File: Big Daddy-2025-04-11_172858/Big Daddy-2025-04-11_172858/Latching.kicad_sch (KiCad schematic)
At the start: 12 parts, among them J1 BMS Button, J2 IMD Button, K2 G5V-2, K3 G5V-2

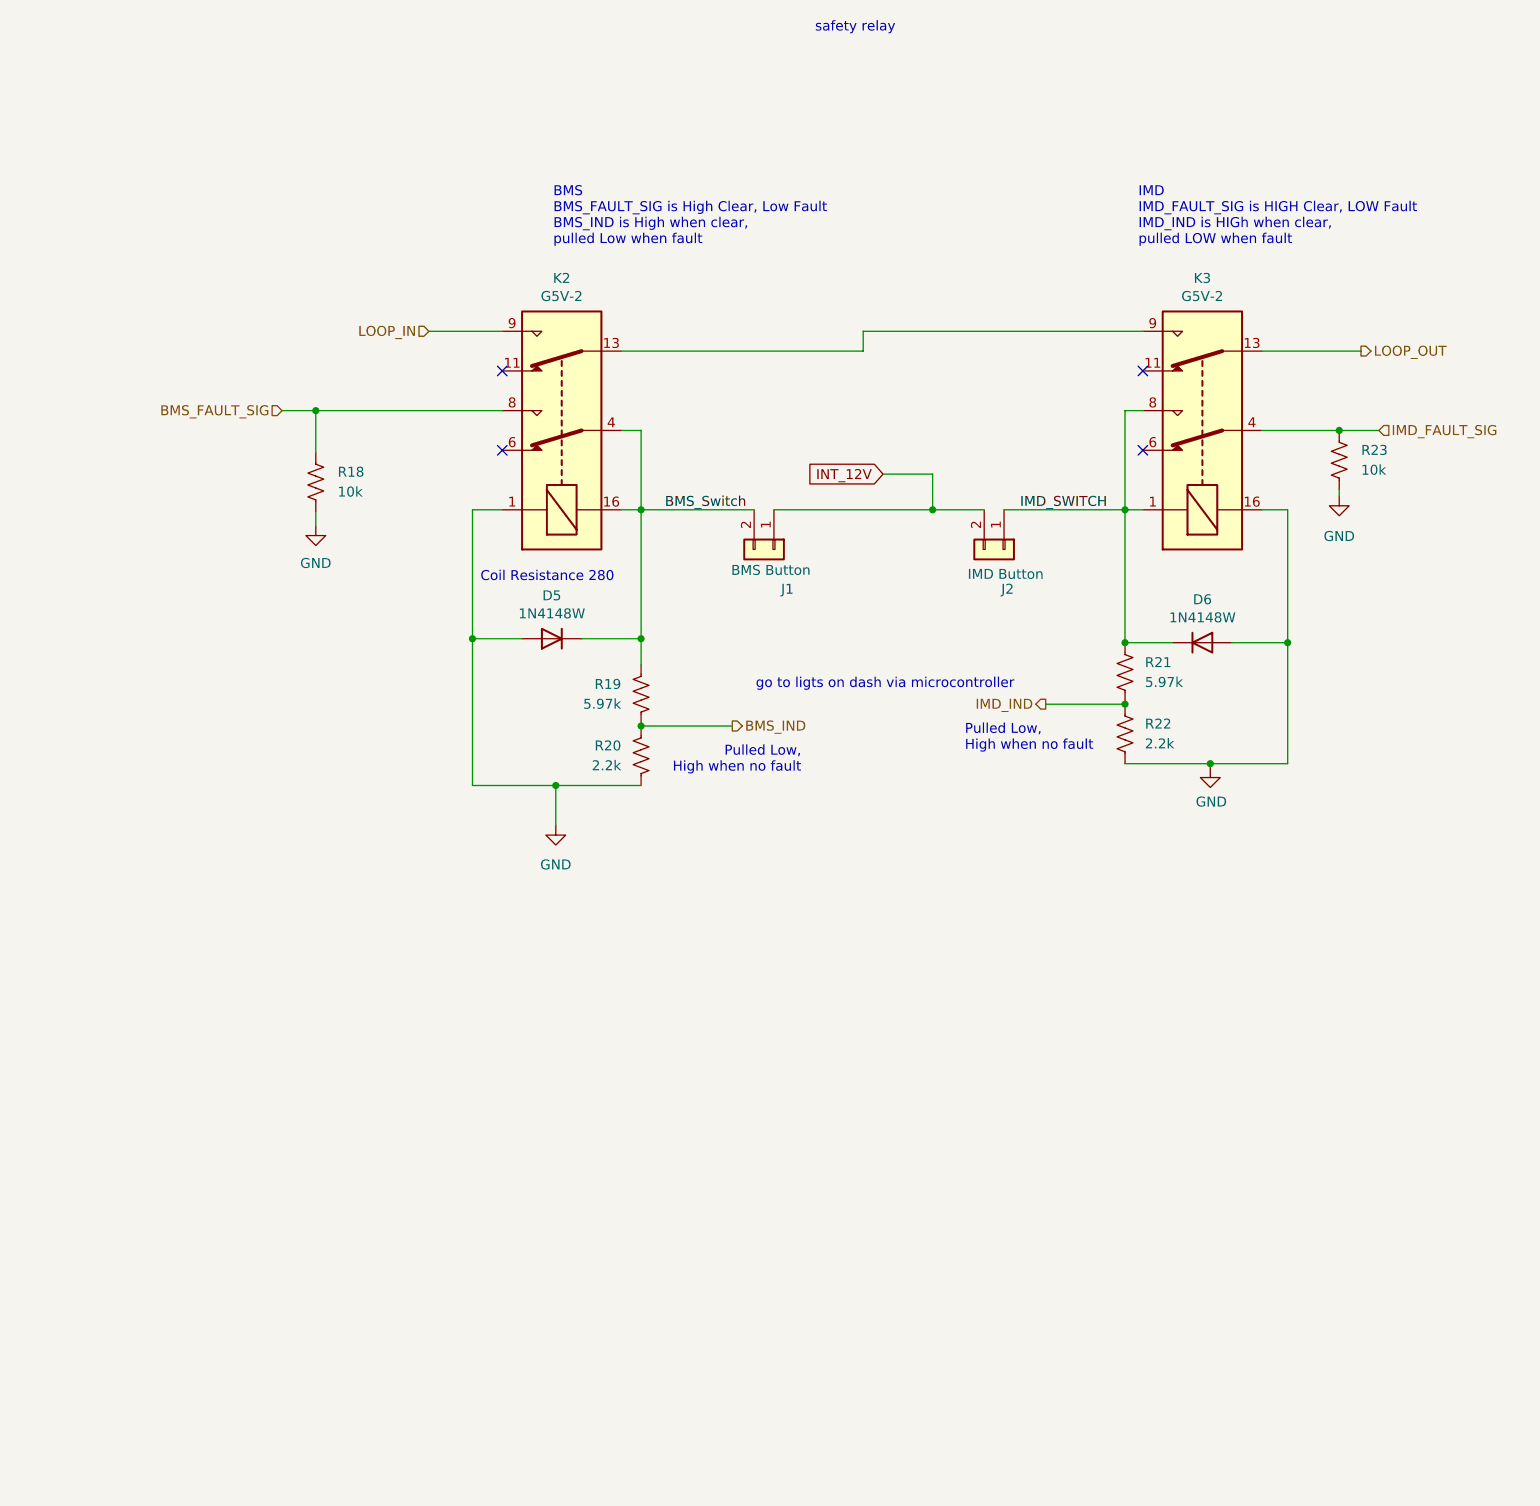
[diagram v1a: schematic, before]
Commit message: changed bms relay
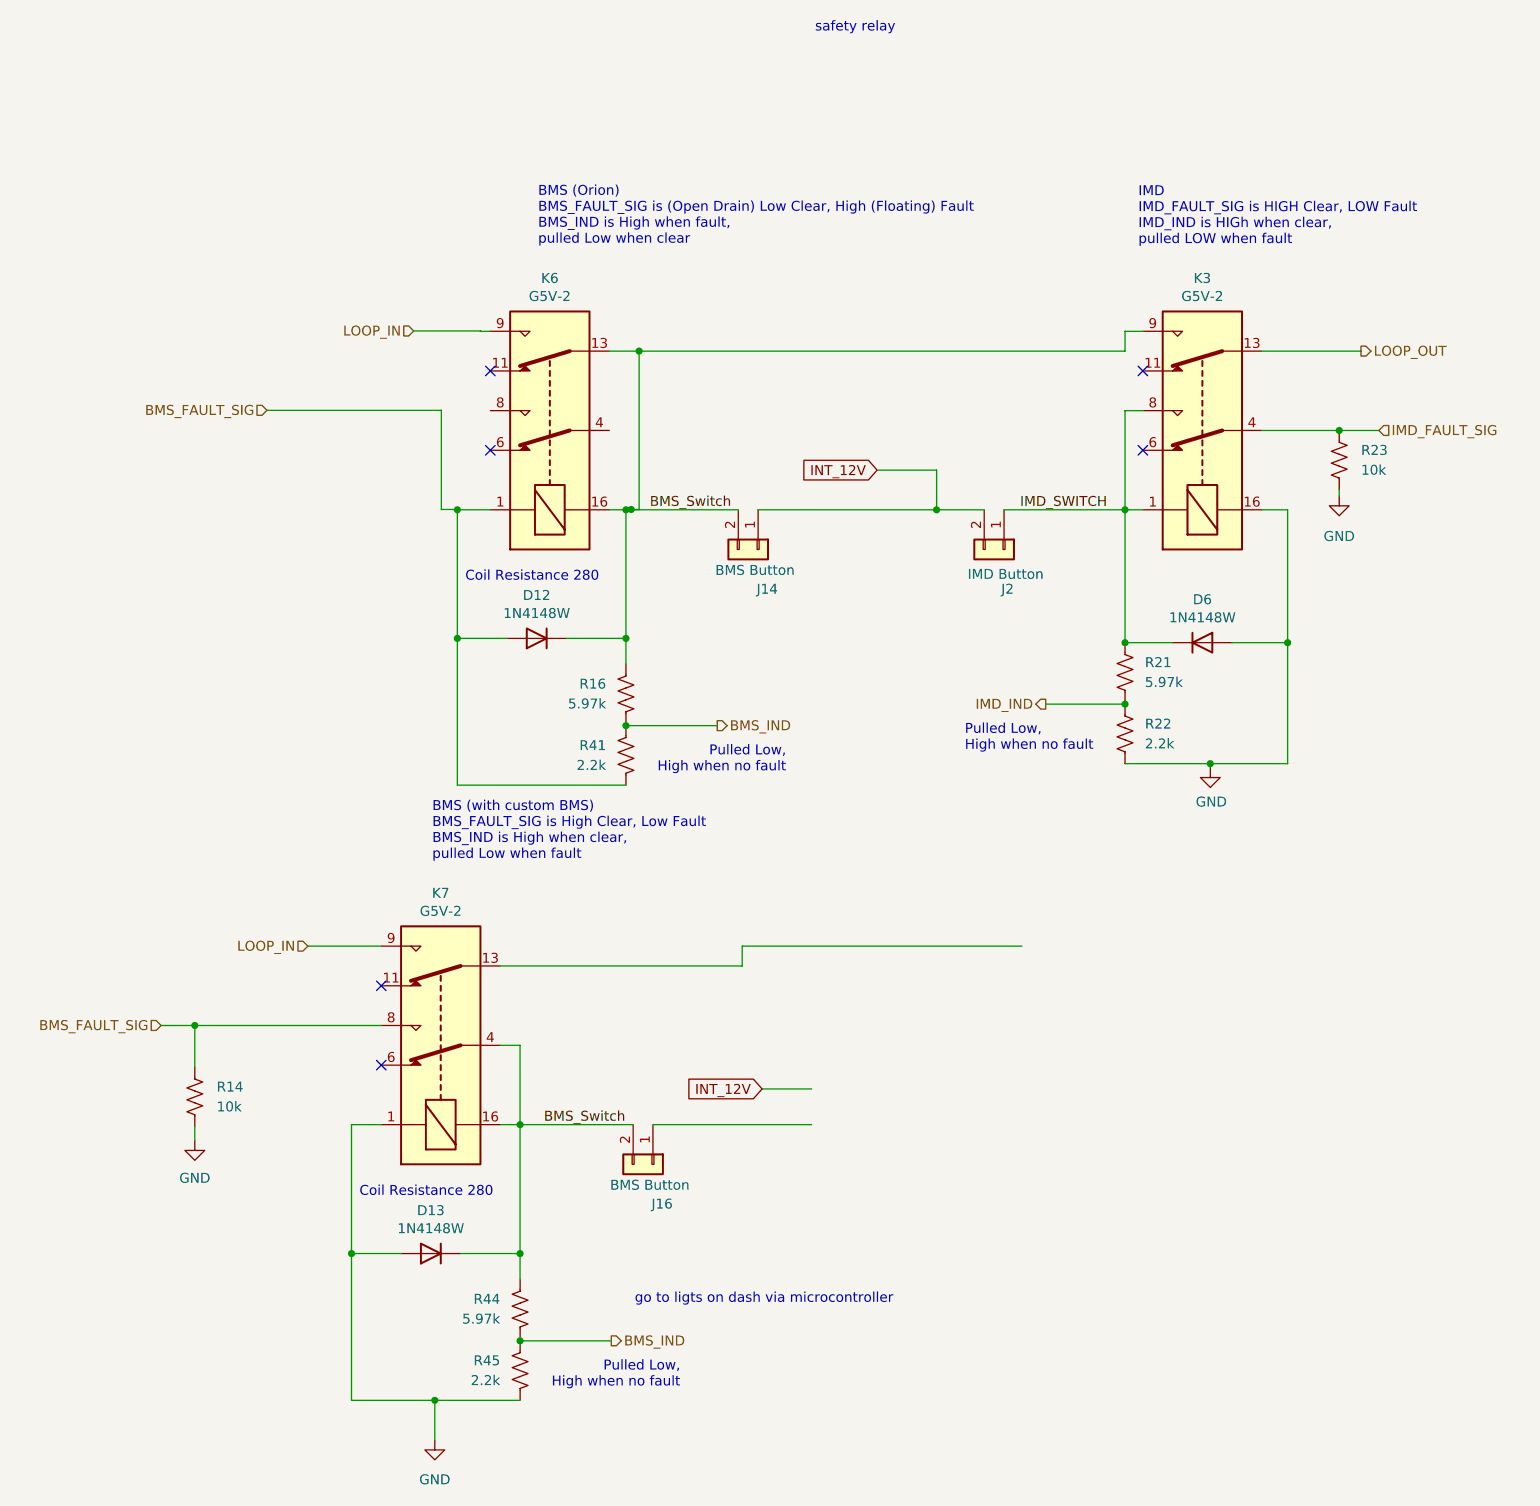
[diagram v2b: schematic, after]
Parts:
- removed D5: 1N4148W, Diode_SMD:D_SOD-123, symbol Diode:1N4148
- removed J1: BMS Button, Connector_JST:JST_XH_B2B-XH-AM_1x02_P2.50mm_Vertical, symbol Connector_Generic:Conn_01x02
- removed K2: G5V-2, Relay_THT:Relay_DPDT_Omron_G5V-2, symbol Relay:G5V-2
- removed R18: 10k, Resistor_SMD:R_0603_1608Metric_Pad0.98x0.95mm_HandSolder, symbol Device:R_US
- removed R19: 5.97k, Resistor_SMD:R_0603_1608Metric_Pad0.98x0.95mm_HandSolder, symbol Device:R_US
- removed R20: 2.2k, Resistor_SMD:R_0603_1608Metric_Pad0.98x0.95mm_HandSolder, symbol Device:R_US
- added D12, D13: 1N4148W, Diode_SMD:D_SOD-123, symbol Diode:1N4148
- added J14, J16: BMS Button, Connector_JST:JST_XH_B2B-XH-AM_1x02_P2.50mm_Vertical, symbol Connector_Generic:Conn_01x02
- added K6, K7: G5V-2, Relay_THT:Relay_DPDT_Omron_G5V-2, symbol Relay:G5V-2
- added R14: 10k, Resistor_SMD:R_0603_1608Metric_Pad0.98x0.95mm_HandSolder, symbol Device:R_US
- added R16, R44: 5.97k, Resistor_SMD:R_0603_1608Metric_Pad0.98x0.95mm_HandSolder, symbol Device:R_US
- added R41, R45: 2.2k, Resistor_SMD:R_0603_1608Metric_Pad0.98x0.95mm_HandSolder, symbol Device:R_US
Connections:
- net BMS_FAULT_SIG: now also D12.2 (A), K6.1, K7.8, R14.1, R41.2
- net BMS_IND: now also R16.2, R41.1, R44.2, R45.1
- net BMS_Switch: now also K3.9, D12.1 (K), D13.1 (K), J14.2 (Pin_2), J16.2 (Pin_2), K6.13, K6.16, K7.16, K7.4, R16.1, R44.1
- net GND: now also D13.2 (A), K7.1, R14.2, R45.2
- net INT_12V: now also J14.1 (Pin_1)
- net LOOP_IN: now also K6.9, K7.9
- no-connect marks 4 -> 6
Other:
- note added: "BMS (Orion) BMS_FAULT_SIG is (Open Drain) Low Clear, High (Floating) Fault BMS_IND is High when fault, pulled Low when clear"
- note added: "BMS (with custom BMS) BMS_FAULT_SIG is High Clear, Low Fault BMS_IND is High when clear, pulled Low when fault"
- note removed: "BMS BMS_FAULT_SIG is High Clear, Low Fault BMS_IND is High when clear, pulled Low when fault"

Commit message: PCB fixes
BMS relay
C12 footprint
TSMP resistor connections
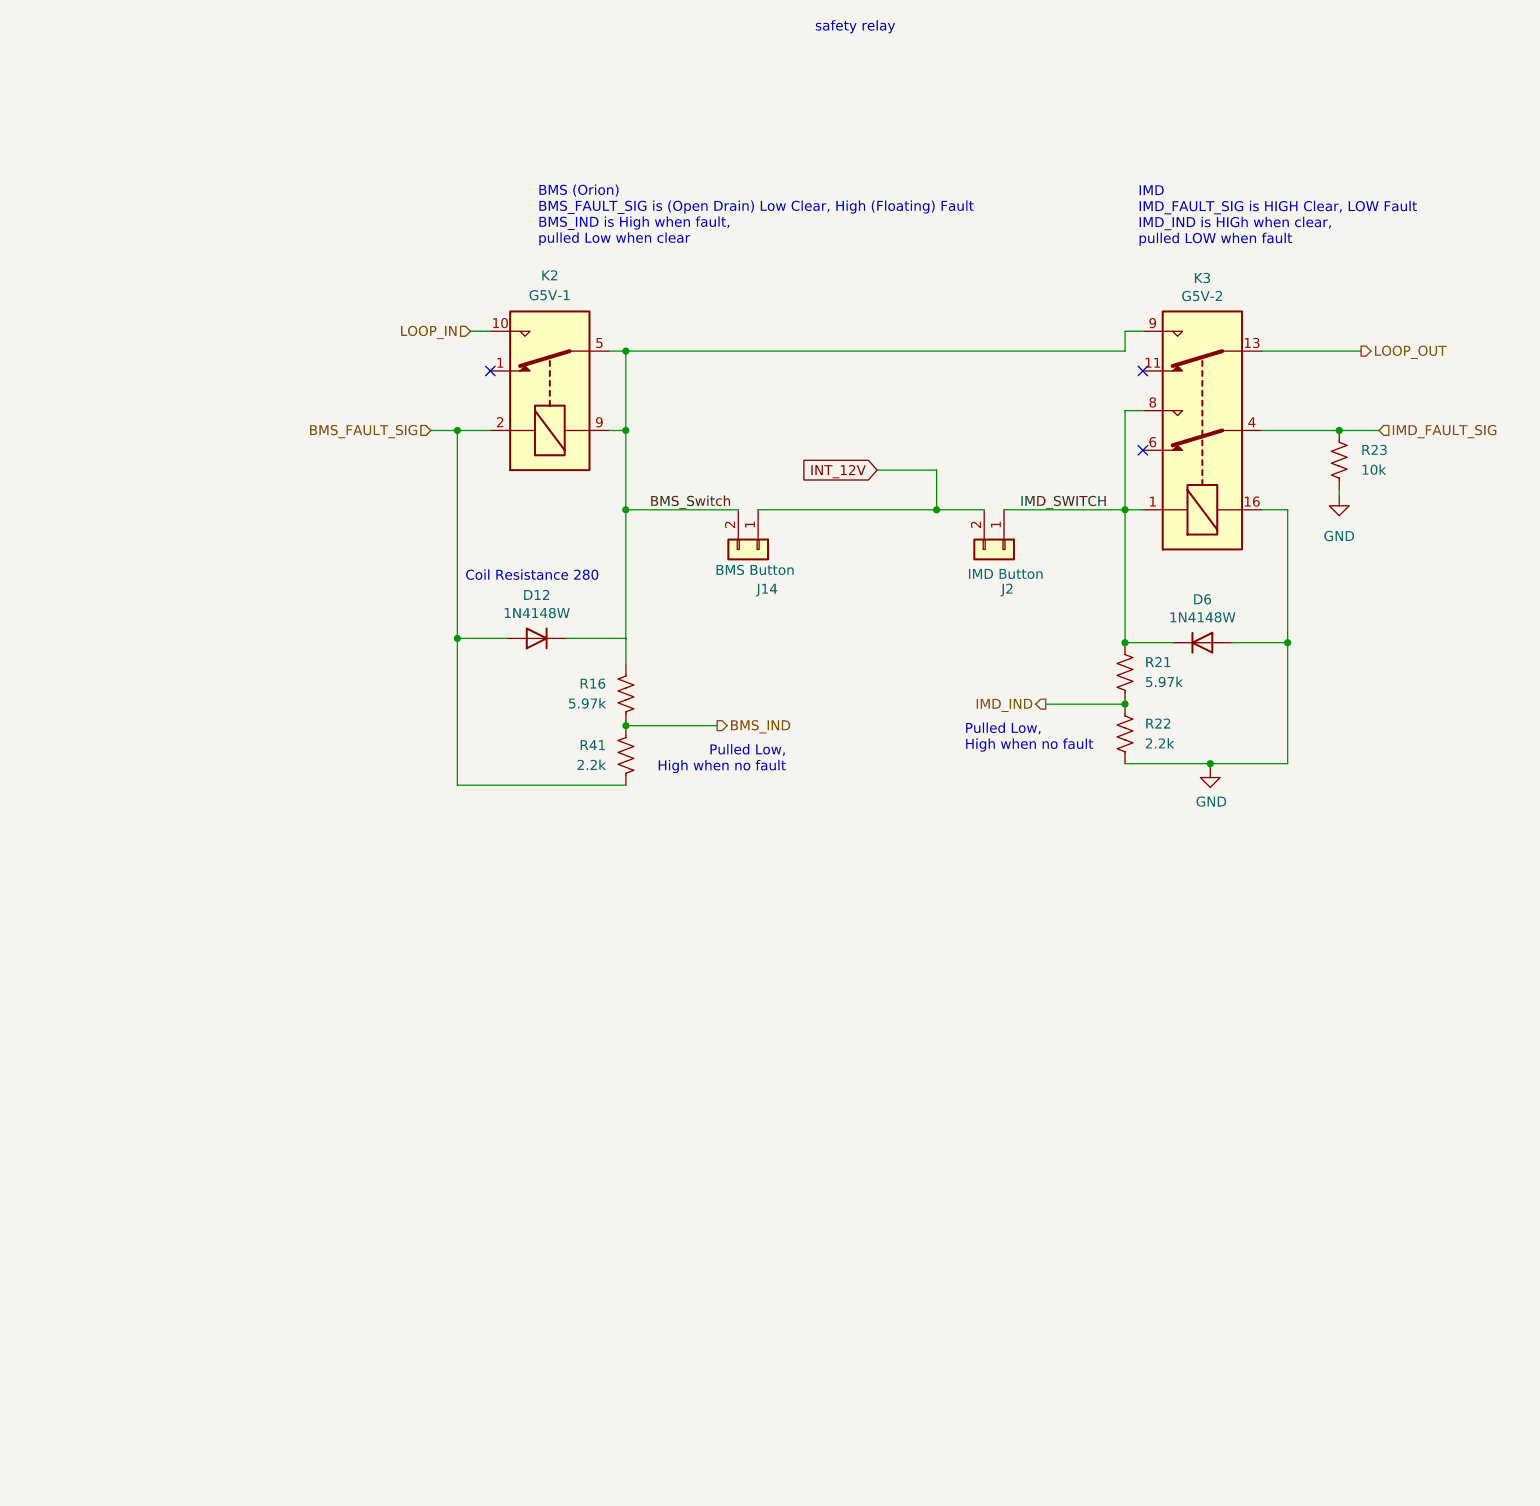
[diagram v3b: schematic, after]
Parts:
- removed D13: 1N4148W, Diode_SMD:D_SOD-123, symbol Diode:1N4148
- removed J16: BMS Button, Connector_JST:JST_XH_B2B-XH-AM_1x02_P2.50mm_Vertical, symbol Connector_Generic:Conn_01x02
- removed K6, K7: G5V-2, Relay_THT:Relay_DPDT_Omron_G5V-2, symbol Relay:G5V-2
- removed R14: 10k, Resistor_SMD:R_0603_1608Metric_Pad0.98x0.95mm_HandSolder, symbol Device:R_US
- removed R44: 5.97k, Resistor_SMD:R_0603_1608Metric_Pad0.98x0.95mm_HandSolder, symbol Device:R_US
- removed R45: 2.2k, Resistor_SMD:R_0603_1608Metric_Pad0.98x0.95mm_HandSolder, symbol Device:R_US
- added K2: G5V-1, Relay_THT:Relay_SPDT_Omron_G5V-1, symbol Relay:G5V-1
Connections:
- net BMS_FAULT_SIG: now also K2.2
- net BMS_Switch: now also K2.5, K2.6, K2.9; no longer D12.1 (K), R16.1
- net LOOP_IN: now also K2.10
- new net: D12.1 (K), R16.1
- no-connect marks 6 -> 3
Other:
- note removed: "BMS (with custom BMS) BMS_FAULT_SIG is High Clear, Low Fault BMS_IND is High when clear, pulled Low when fault"
- note removed: "go to ligts on dash via microcontroller"
